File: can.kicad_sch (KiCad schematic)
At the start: 11 parts, among them U201 SN65HVD230

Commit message: File names and ERC
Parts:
- renumbered C201 to C15, C202 to C16, C204 to C17, C203 to C18, C205 to C19, D201 to D1, JP201 to JP1, R201 to R10, R202 to R8, R203 to R9, U201 to U2

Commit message: Some routing
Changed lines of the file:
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@@
     (effects (font (size 1.27 1.27)) (justify left))
   )
-  (hierarchical_label "CAN_LOW" (shape bidirectional) (at 175.26 97.79 0) (fields_autoplaced)
-    (effects (font (size 1.27 1.27)) (justify left))
+  (hierarchical_label "CAN_LOW" (shape bidirectional) (at 175.26 97.79 180) (fields_autoplaced)
+    (effects (font (size 1.27 1.27)) (justify right))
   )
   (symbol (lib_id "power:GND") (at 134.62 99.06 0) (unit 1)
@@
     )
   )
-  (symbol (lib_id "Device:R_Small") (at 124.46 95.25 0) (unit 1)
+  (symbol (lib_id "Device:R_Small") (at 124.46 95.25 0) (mirror y) (unit 1)
     (in_bom yes) (on_board yes) (dnp no)
-    (property "Reference" "R10" (at 118.11 93.98 0)
-      (effects (font (size 1.27 1.27)) (justify left))
-    )
-    (property "Value" "0" (at 118.11 96.52 0)
+    (property "Reference" "R10" (at 130.81 93.98 0)
+      (effects (font (size 1.27 1.27)) (justify left))
+    )
+    (property "Value" "0" (at 130.81 96.52 0)
       (effects (font (size 1.27 1.27)) (justify left))
     )
@@
   )
   (symbol (lib_id "Device:R") (at 167.64 93.98 0) (unit 1)
-    (in_bom yes) (on_board yes) (dnp no) (fields_autoplaced)
+    (in_bom yes) (on_board yes) (dnp no)
     (property "Reference" "R9" (at 162.56 92.71 0)
-      (effects (font (size 1.27 1.27)) (justify left))
+      (effects (font (size 1.27 1.27)) (justify right))
     )
     (property "Value" "60" (at 162.56 95.25 0)

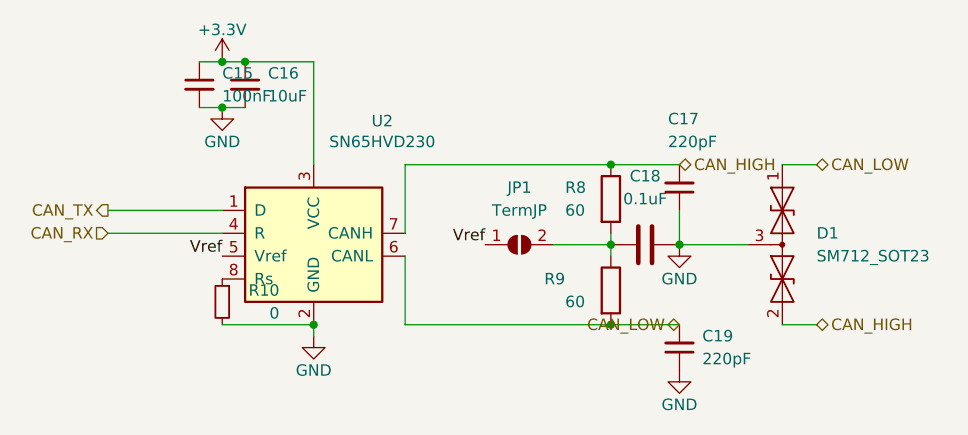
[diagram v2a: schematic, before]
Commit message: Camera buck changes, c and r footprints, other
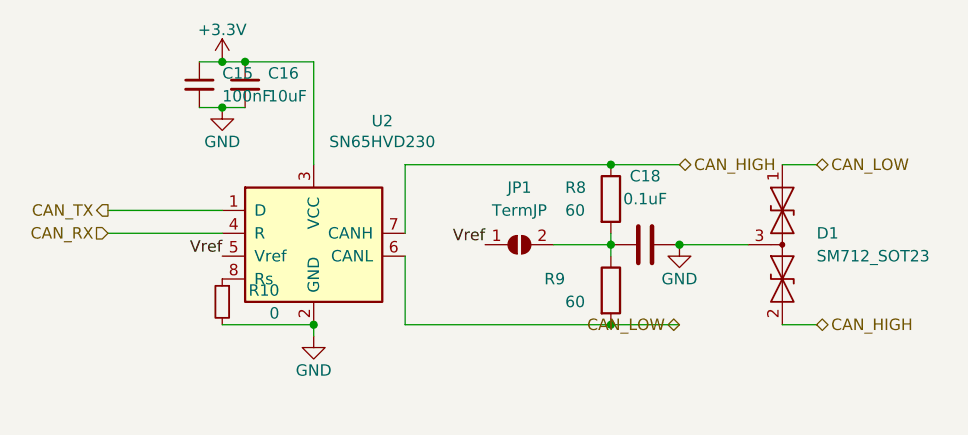
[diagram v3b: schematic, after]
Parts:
- removed C17, C19: 220pF, Capacitor_SMD:C_0402_1005Metric, symbol Device:C_Small
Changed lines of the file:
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@@
-    (stroke (width 0) (type default))
-  )
-  (wire (pts (xy 175.26 85.09) (xy 175.26 88.9))
     (stroke (width 0) (type default))
   )
@@
     )
   )
-  (symbol (lib_id "Device:C_Small") (at 175.26 82.55 180) (unit 1)
-    (in_bom yes) (on_board yes) (dnp no)
-    (property "Reference" "C17" (at 173.99 74.93 0)
-      (effects (font (size 1.27 1.27)) (justify right))
-    )
-    (property "Value" "220pF" (at 173.99 77.47 0)
-      (effects (font (size 1.27 1.27)) (justify right))
-    )
-    (property "Footprint" "Capacitor_SMD:C_0402_1005Metric" (at 175.26 82.55 0)
-      (effects (font (size 1.27 1.27)) hide)
-    )
-    (property "Datasheet" "~" (at 175.26 82.55 0)
-      (effects (font (size 1.27 1.27)) hide)
-    )
-    (pin "1")
-    (pin "2")
-    (instances
-      (project "RicardoCHEESE"
-        (path "/7db990e4-92e1-4f99-b4d2-435bbec1ba83/00000000-0000-0000-0000-000061942b9a"
-          (reference "C17") (unit 1)
-        )
-      )
-    )
-  )
   (symbol (lib_id "Diode:SM712_SOT23") (at 186.69 88.9 270) (unit 1)
     (in_bom yes) (on_board yes) (dnp no) (fields_autoplaced)
@@
         (path "/7db990e4-92e1-4f99-b4d2-435bbec1ba83/00000000-0000-0000-0000-000061942b9a"
           (reference "#PWR026") (unit 1)
-        )
-      )
-    )
-  )
-  (symbol (lib_id "power:GND") (at 175.26 102.87 0) (unit 1)
-    (in_bom yes) (on_board yes) (dnp no) (fields_autoplaced)
-    (property "Reference" "#PWR028" (at 175.26 109.22 0)
-      (effects (font (size 1.27 1.27)) hide)
-    )
-    (property "Value" "GND" (at 175.26 106.68 0)
-      (effects (font (size 1.27 1.27)))
-    )
-    (property "Footprint" "" (at 175.26 102.87 0)
-      (effects (font (size 1.27 1.27)) hide)
-    )
-    (property "Datasheet" "" (at 175.26 102.87 0)
-      (effects (font (size 1.27 1.27)) hide)
-    )
-    (pin "1")
-    (instances
-      (project "RicardoCHEESE"
-        (path "/7db990e4-92e1-4f99-b4d2-435bbec1ba83/00000000-0000-0000-0000-000061942b9a"
-          (reference "#PWR028") (unit 1)
         )
       )
@@
         )
       )
-    )
-  )
-  (symbol (lib_id "Device:C_Small") (at 175.26 100.33 180) (unit 1)
-    (in_bom yes) (on_board yes) (dnp no) (fields_autoplaced)
-    (property "Reference" "C19" (at 177.8 99.0535 0)
-      (effects (font (size 1.27 1.27)) (justify right))
-    )
-    (property "Value" "220pF" (at 177.8 101.5935 0)
-      (effects (font (size 1.27 1.27)) (justify right))
-    )
-    (property "Footprint" "Capacitor_SMD:C_0402_1005Metric" (at 175.26 100.33 0)
-      (effects (font (size 1.27 1.27)) hide)
-    )
-    (property "Datasheet" "~" (at 175.26 100.33 0)
-      (effects (font (size 1.27 1.27)) hide)
-    )
-    (pin "1")
-    (pin "2")
-    (instances
-      (project "RicardoCHEESE"
-        (path "/7db990e4-92e1-4f99-b4d2-435bbec1ba83/00000000-0000-0000-0000-000061942b9a"
-          (reference "C19") (unit 1)
-        )
-      )

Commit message: post andrei review
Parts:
- C16: footprint Capacitor_SMD:C_0603_1608Metric -> Capacitor_SMD:C_0402_1005Metric
- C18: value 0.1uF -> 47nF
- R8, R9: footprint Resistor_SMD:R_0402_1005Metric -> Resistor_SMD:R_0603_1608Metric
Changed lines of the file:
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@@
       (effects (font (size 1.27 1.27)) (justify left))
     )
-    (property "Footprint" "Capacitor_SMD:C_0603_1608Metric" (at 127 71.12 0)
+    (property "Footprint" "Capacitor_SMD:C_0402_1005Metric" (at 127 71.12 0)
       (effects (font (size 1.27 1.27)) hide)
     )
@@
       (effects (font (size 1.27 1.27)) (justify left))
     )
-    (property "Footprint" "Resistor_SMD:R_0402_1005Metric" (at 165.862 93.98 90)
+    (property "Footprint" "Resistor_SMD:R_0603_1608Metric" (at 165.862 93.98 90)
       (effects (font (size 1.27 1.27)) hide)
     )
@@
       (effects (font (size 1.27 1.27)) (justify left))
     )
-    (property "Footprint" "Resistor_SMD:R_0402_1005Metric" (at 165.862 83.82 90)
+    (property "Footprint" "Resistor_SMD:R_0603_1608Metric" (at 165.862 83.82 90)
       (effects (font (size 1.27 1.27)) hide)
     )
@@
       (effects (font (size 1.27 1.27)))
     )
-    (property "Value" "0.1uF" (at 171.45 83.82 90)
+    (property "Value" "47nF" (at 171.45 83.82 90)
       (effects (font (size 1.27 1.27)))
     )
